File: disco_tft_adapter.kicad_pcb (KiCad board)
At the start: 4 copper layers, 127 x 116.1 mm, 22 parts, among them J1 QTH-030-02-L-D-A, J2 F31L-1A7H1-11030

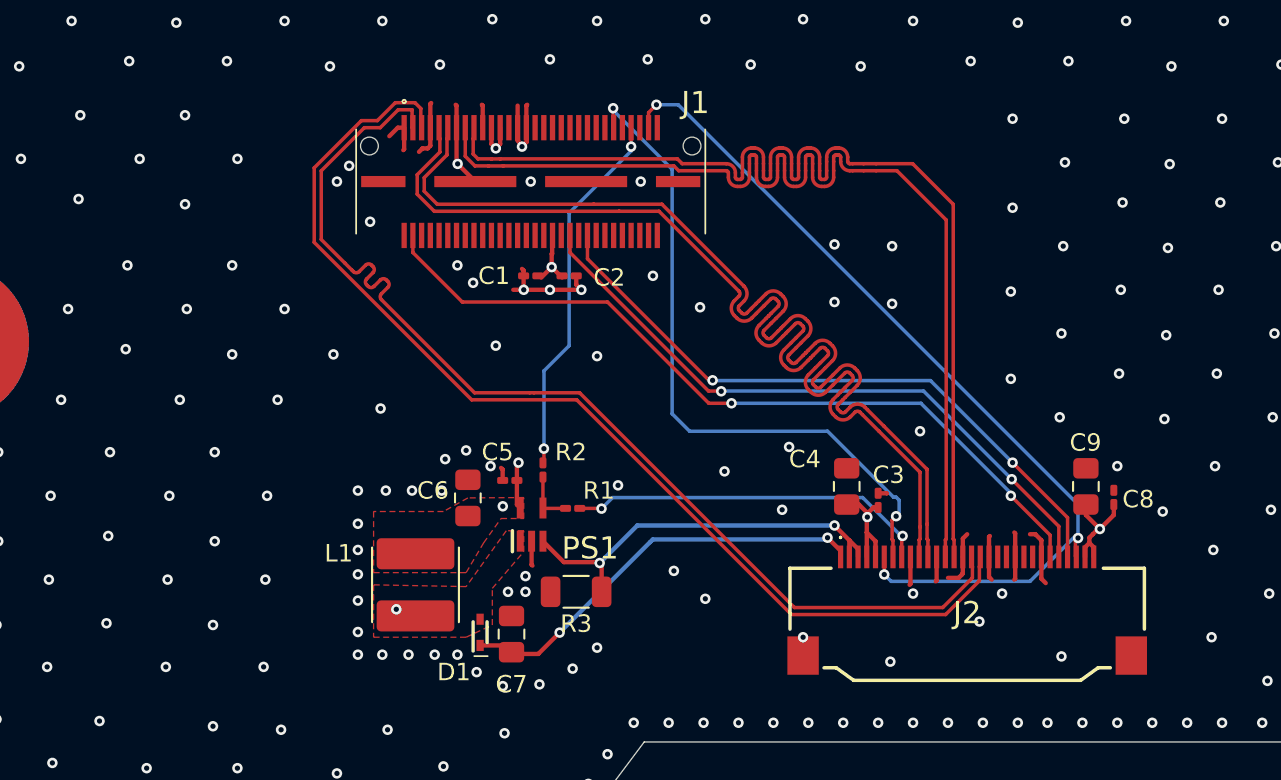
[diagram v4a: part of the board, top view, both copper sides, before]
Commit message: [layout] some finishing touches after gerber review
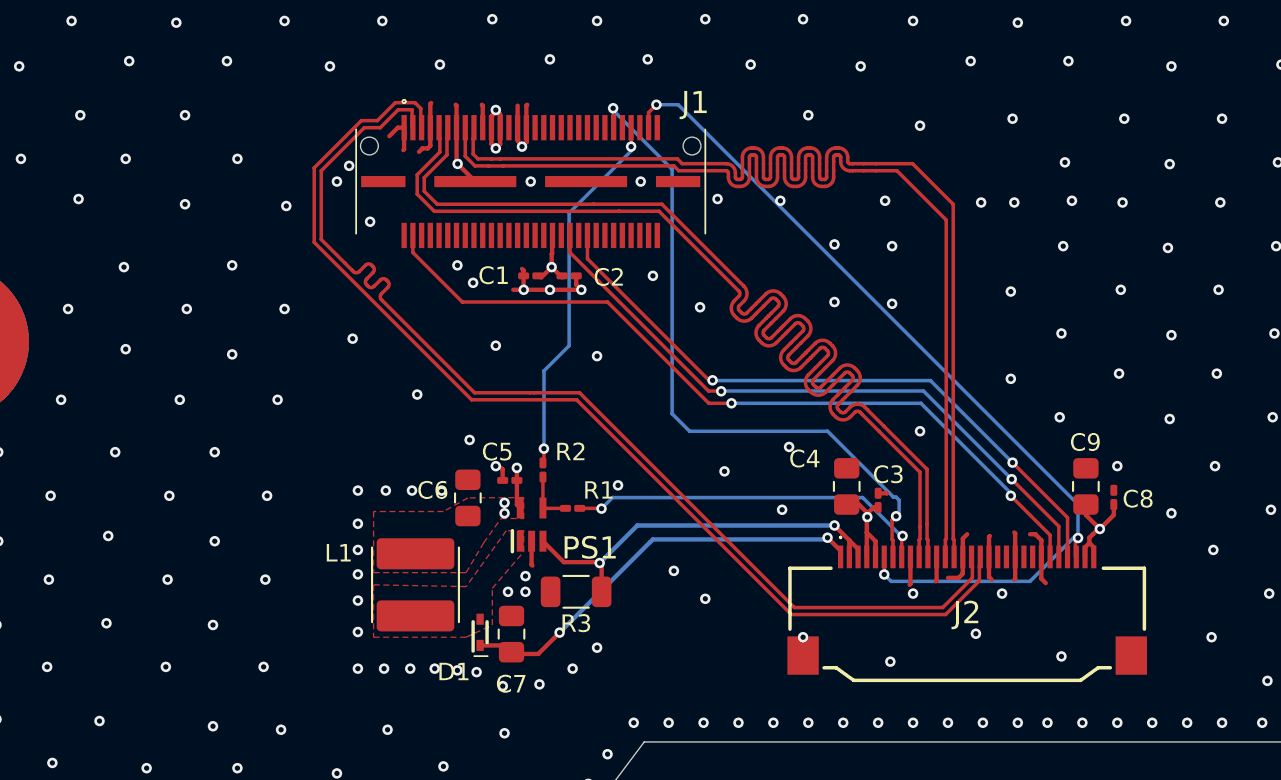
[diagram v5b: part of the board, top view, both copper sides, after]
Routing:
- net VCC_BL: track 5.30 -> 7.19 mm, vias 3 -> 5
- net GND: vias 775 -> 781
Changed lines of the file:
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@@
 			(net 3 "GND")
 			(pintype "passive")
+			(zone_connect 2)
 		)
 		(embedded_fonts no)
@@
 			(net 3 "GND")
 			(pintype "passive")
+			(zone_connect 2)
 		)
 		(embedded_fonts no)
@@
 	)
 	(via
-		(at 72.8 111.5)
+		(at 63.7 97)
 		(size 0.6)
 		(drill 0.3)
@@
 	)
 	(via
-		(at 73.5 122.7)
+		(at 73.5 123.6)
 		(size 0.6)
 		(drill 0.3)
@@
 	)
 	(via
-		(at 69.2 122.7)
+		(at 69.3 123.5)
 		(size 0.6)
 		(drill 0.3)
@@
 	)
 	(via
+		(at 103.5 96.8)
+		(size 0.6)
+		(drill 0.3)
+		(layers "F.Cu" "B.Cu")
+		(free yes)
+		(net 3)
+	)
+	(via
 		(at 49.2 82.2)
 		(size 0.6)
@@
 	)
 	(via
-		(at 72.2 122.7)
+		(at 72.2 123.5)
 		(size 0.6)
 		(drill 0.3)
@@
 	)
 	(via
-		(at 103.4 120.8)
+		(at 103.2 121.5)
 		(size 0.6)
 		(drill 0.3)
@@
 	)
 	(via
+		(at 98 96.7)
+		(size 0.6)
+		(drill 0.3)
+		(layers "F.Cu" "B.Cu")
+		(free yes)
+		(net 3)
+	)
+	(via
 		(at 140.7 126.4)
 		(size 0.6)
@@
 	)
 	(via
-		(at 74 111)
+		(at 74.2 110.4)
 		(size 0.6)
 		(drill 0.3)
@@
 	)
 	(via
-		(at 113.9 114.5)
+		(at 114.4 114.6)
 		(size 0.6)
 		(drill 0.3)
@@
 	)
 	(via
+		(at 88.4 96.6)
+		(size 0.6)
+		(drill 0.3)
+		(layers "F.Cu" "B.Cu")
+		(free yes)
+		(net 3)
+	)
+	(via
 		(at 114.5 79)
 		(size 0.6)
@@
 	)
 	(via
+		(at 100 92.4)
+		(size 0.6)
+		(drill 0.3)
+		(layers "F.Cu" "B.Cu")
+		(free yes)
+		(net 3)
+	)
+	(via
 		(at 152.9 136.2)
 		(size 0.6)
@@
 	)
 	(via
-		(at 114 109.2)
+		(at 114.3 109.2)
 		(size 0.6)
 		(drill 0.3)
@@
 	)
 	(via
-		(at 70.7 122.7)
+		(at 70.8 123.5)
 		(size 0.6)
 		(drill 0.3)
@@
 	)
 	(via
-		(at 55.3 94.3)
+		(at 54.5 94.3)
 		(size 0.6)
 		(drill 0.3)
@@
 	)
 	(via
-		(at 70 120.1)
-		(size 0.6)
-		(drill 0.3)
-		(layers "F.Cu" "B.Cu")
-		(free yes)
-		(net 3)
-	)
-	(via
 		(at 135 131.4)
 		(size 0.6)
@@
 	)
 	(via
-		(at 54.6 100.4)
+		(at 54.4 100.5)
 		(size 0.6)
 		(drill 0.3)
@@
 	)
 	(via
+		(at 108.7 96.7)
+		(size 0.6)
+		(drill 0.3)
+		(layers "F.Cu" "B.Cu")
+		(free yes)
+		(net 3)
+	)
+	(via
 		(at 150.2 94.4)
 		(size 0.6)
@@
 	)
 	(via
-		(at 69.1 108.6)
+		(at 71.2 107.8)
 		(size 0.6)
 		(drill 0.3)
@@
 	)
 	(via
-		(at 105.3 97.1)
+		(at 105.4 96.8)
 		(size 0.6)
 		(drill 0.3)
@@
 	)
 	(via
+		(at 93.6 91.8)
+		(size 0.6)
+		(drill 0.3)
+		(layers "F.Cu" "B.Cu")
+		(free yes)
+		(net 3)
+	)
+	(via
 		(at 140.8 121.6)
 		(size 0.6)
@@
 	)
 	(via
+		(at 92 96.7)
+		(size 0.6)
+		(drill 0.3)
+		(layers "F.Cu" "B.Cu")
+		(free yes)
+		(net 3)
+	)
+	(via
 		(at 150.4 78.3)
 		(size 0.6)
@@
 	)
 	(via
-		(at 75.4 111.9)
+		(at 75.7 111.9)
 		(size 0.6)
 		(drill 0.3)
@@
 	)
 	(via
-		(at 53.6 111.1)
+		(at 53.9 111.1)
 		(size 0.6)
 		(drill 0.3)
@@
 	)
 	(via
-		(at 67.8 122.7)
+		(at 67.8 123.5)
 		(size 0.6)
 		(drill 0.3)
@@
 	)
 	(via
-		(at 114.1 104.4)
+		(at 114.4 104.4)
 		(size 0.6)
 		(drill 0.3)
@@
 	)
 	(via
-		(at 66.4 105.5)
+		(at 67.5 104.6)
 		(size 0.6)
 		(drill 0.3)
@@
 	)
 	(segment
-		(start 76.9075 112.72)
-		(end 76.9075 111.7925)
+		(start 75.7 91.5)
+		(end 75.7 91.6)
 		(width 0.25)
 		(layer "F.Cu")
@@
 	)
 	(segment
-		(start 76.9075 111.7925)
-		(end 77 111.7)
+		(start 76.9075 112)
+		(end 76.9075 112.72)
+		(width 0.25)
+		(layer "F.Cu")
+		(net 20)
+	)
+	(segment
+		(start 75.7 91.6)
+		(end 75.45 91.85)
+		(width 0.25)
+		(layer "F.Cu")
+		(net 20)
+	)
+	(segment
+		(start 75.7 91.5)
+		(end 75.95 91.75)
+		(width 0.25)
+		(layer "F.Cu")
+		(net 20)
+	)
+	(segment
+		(start 75.45 91.85)
+		(end 75.45 92.514)
 		(width 0.25)
 		(layer "F.Cu")
@@
 		(net 20)
 	)
+	(segment
+		(start 75.95 91.75)
+		(end 75.95 92.514)
+		(width 0.25)
+		(layer "F.Cu")
+		(net 20)
+	)
 	(via
-		(at 77 111.7)
+		(at 76.9075 112)
 		(size 0.6)
 		(drill 0.3)
@@
 	)
 	(via
-		(at 76.1 114.2)
+		(at 75.7 91.5)
+		(size 0.6)
+		(drill 0.3)
+		(layers "F.Cu" "B.Cu")
+		(net 20)
+	)
+	(via
+		(at 76.2 114.6)
+		(size 0.6)
+		(drill 0.3)
+		(layers "F.Cu" "B.Cu")
+		(free yes)
+		(net 20)
+	)
+	(via
+		(at 76.2 114)
 		(size 0.6)
 		(drill 0.3)
@@
 		(polygon
 			(pts
-				(xy 69 116.7) (xy 74.7 116.7) (xy 76 115.8) (xy 76 112.6) (xy 78 111.9) (xy 78 110) (xy 76 108.62)
-				(xy 69 108.62)
+				(xy 68.68162 122.3) (xy 74.38162 122.3) (xy 75.68162 121.4) (xy 75.68162 118.2) (xy 77.68162 117.5)
+				(xy 77.68162 115.6) (xy 75.68162 114.22) (xy 68.68162 114.22)
 			)
 		)

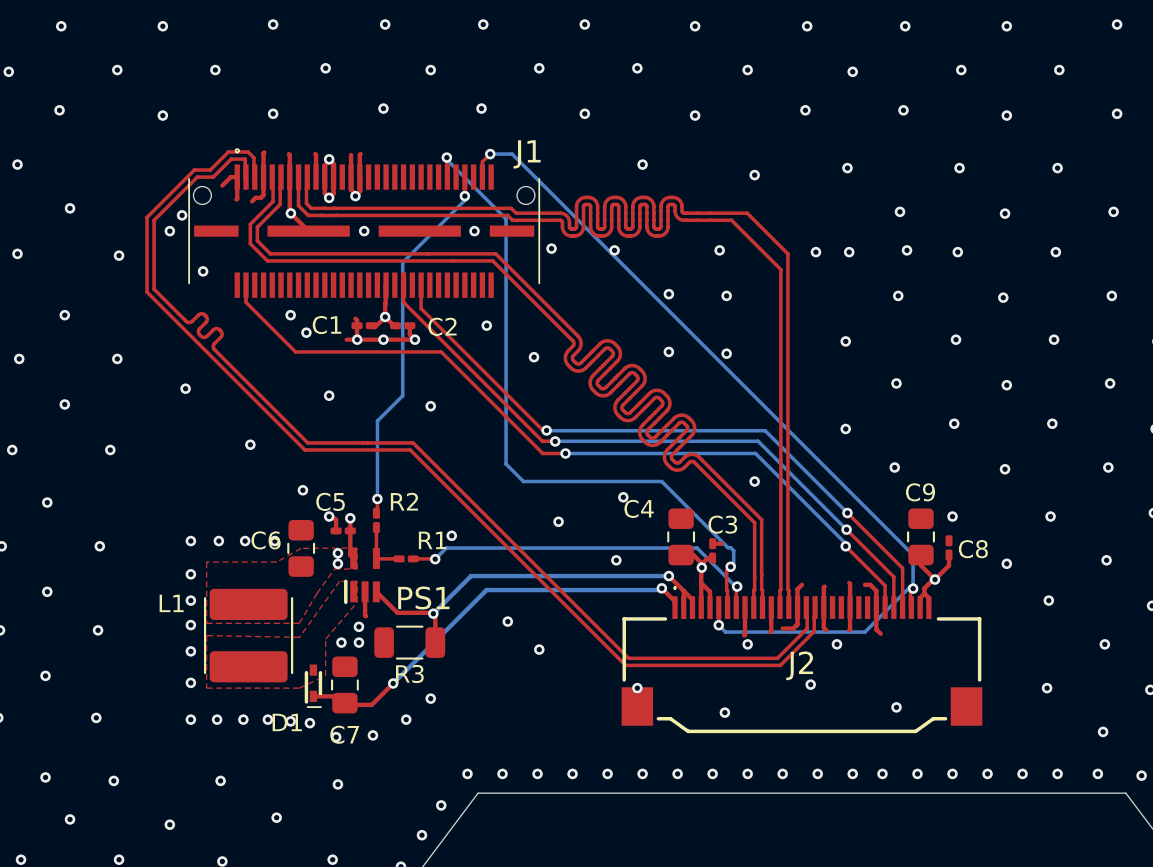
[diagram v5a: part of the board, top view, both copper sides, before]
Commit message: [layout] update footprints, clear routing for tft connector
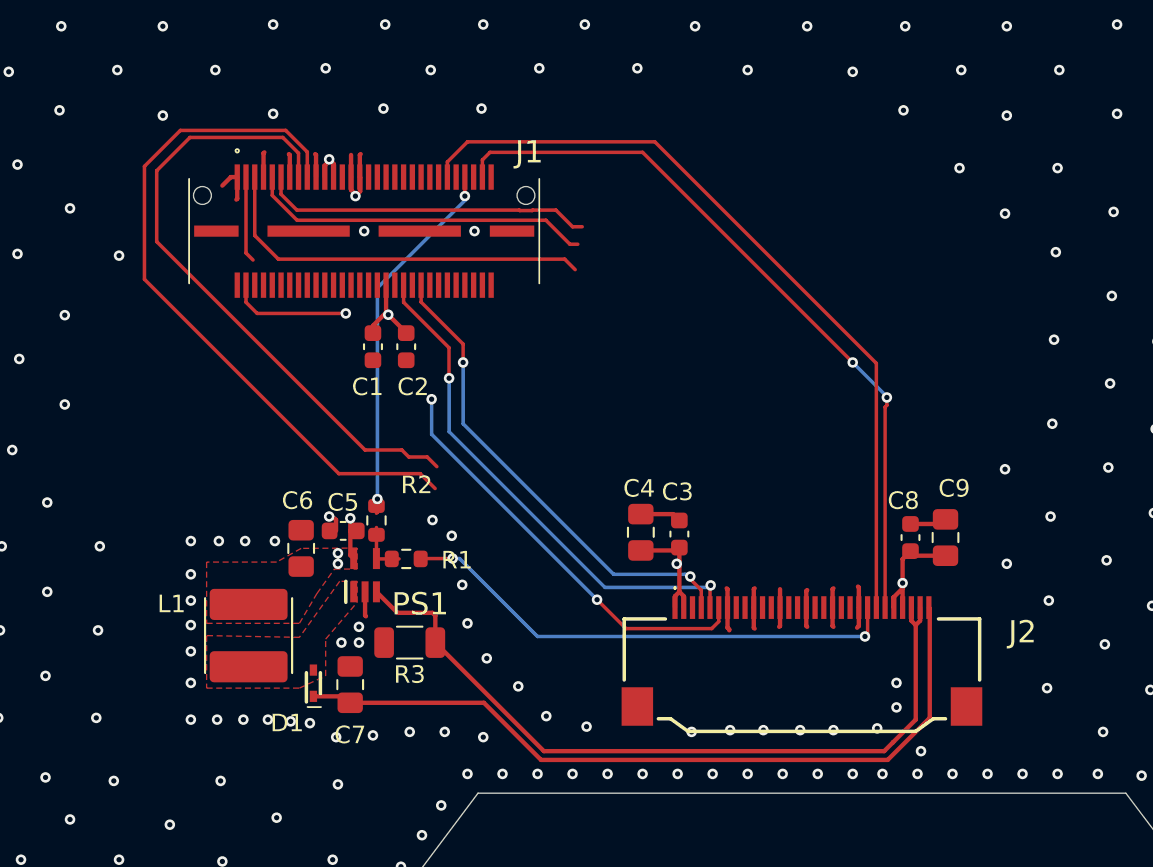
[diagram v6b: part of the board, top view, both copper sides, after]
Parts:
- C1, C2, C3, C5, C8: footprint Capacitor_SMD:C_0201_0603Metric_Pad0.64x0.40mm_HandSolder -> Capacitor_SMD:C_0603_1608Metric
- R1, R2: footprint Resistor_SMD:R_0201_0603Metric_Pad0.64x0.40mm_HandSolder -> Resistor_SMD:R_0603_1608Metric
- moved C4 2.31 mm to (93.5, 112.8)
- moved C8 2.28 mm to (108.9, 113.1)
- moved C3 2.13 mm to (95.7, 112.9)
- moved C9 1.40 mm to (110.9, 113.1)
- moved C1 1.30 mm to (78.2, 102.2), turned to -90 degrees
- moved C2 1.22 mm to (80.1, 102.2), turned to -90 degrees
- moved C7 0.30 mm to (76.9, 121.5)
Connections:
- J2 pad 10: /DSI_D0_P -> unconnected-(J2-Pad10)
- J2 pad 11: /DSI_D0_N -> unconnected-(J2-Pad11)
- J2 pad 13: /DSI_D1_P -> /DSI_D0_P
- J2 pad 14: /DSI_D1_N -> /DSI_D0_N
- J2 pad 22: unconnected-(J2-Pad22) -> /DSI_D1_P
- J2 pad 23: unconnected-(J2-Pad23) -> /DSI_D1_N
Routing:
- net /DSI_CLK_P: track 62.7 -> 4.90 mm
- net /DSI_D0_N: track 62.0 -> 19.0 mm
- net /DSI_D0_P: track 62.0 -> 19.7 mm
- net /DSI_CLK_N: track 62.3 -> 22.4 mm
- net /DSI_D1_P: track 62.4 -> 36.6 mm
- net /DSI_D1_N: track 62.1 -> 40.1 mm
- net /LEDK: track 23.6 -> 43.8 mm, vias 2 -> 0
- net /LEDA: track 24.3 -> 44.0 mm, vias 2 -> 0
- net /CTP_SCL: track 37.4 -> 27.5 mm
- net /RST: track 51.6 -> 42.1 mm, vias 3 -> 2
- net GND: track 40.6 -> 31.9 mm, vias 781 -> 740
- net /PWM_DISP: track 20.9 -> 28.9 mm
- net /CTP_SDA: track 37.2 -> 29.4 mm
- net /CTP_INT: track 45.5 -> 37.8 mm, vias 2 -> 3
- net /TE: track 39.1 -> 45.0 mm, vias 2 -> 0
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
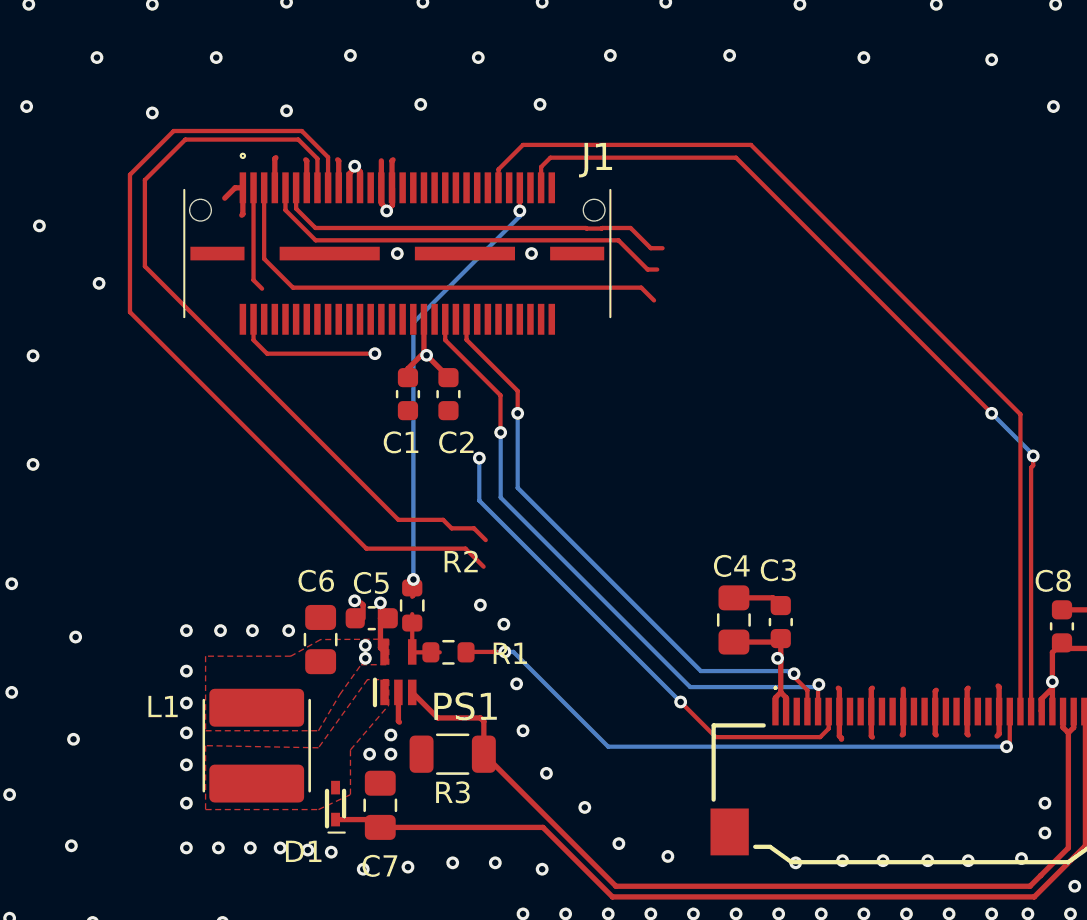
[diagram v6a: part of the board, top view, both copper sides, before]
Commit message: [layout] route display TFT plug
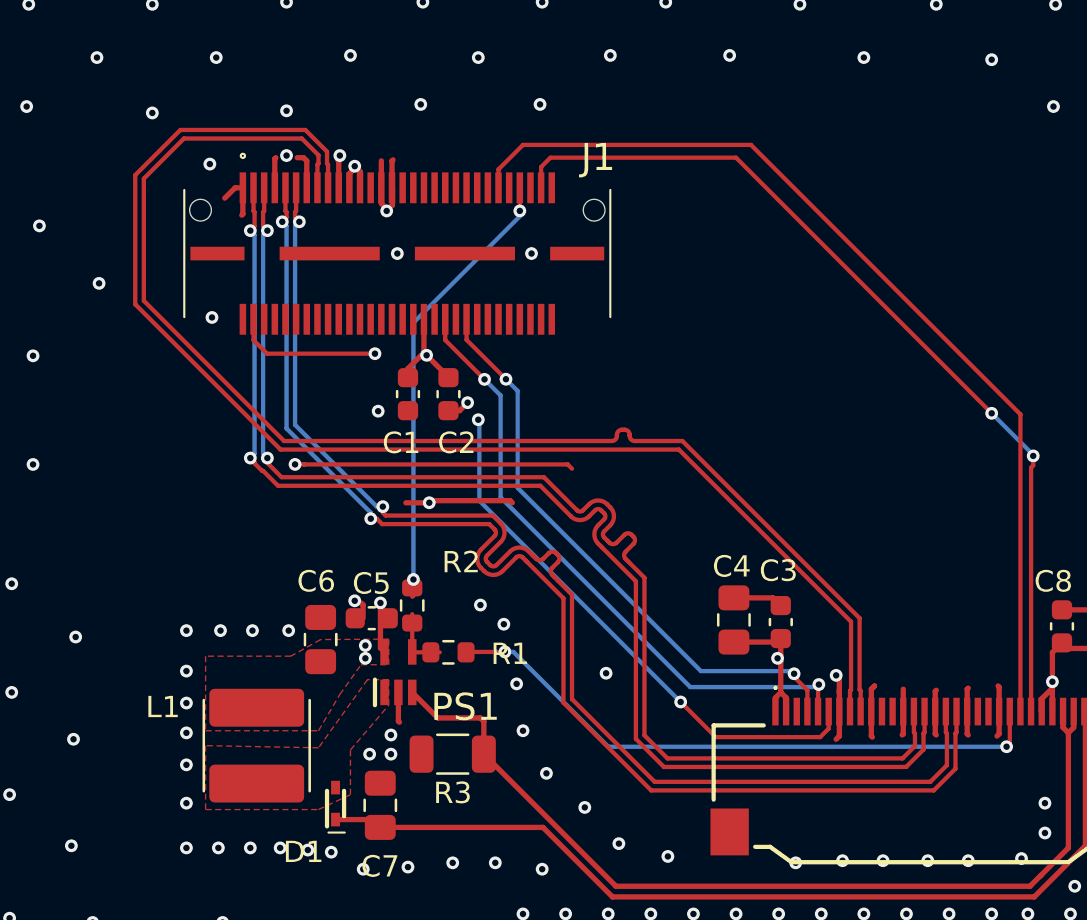
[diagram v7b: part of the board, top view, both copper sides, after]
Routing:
- net /DSI_CLK_P: track 4.90 -> 58.7 mm, vias 0 -> 2
- net /DSI_D0_N: track 19.0 -> 58.7 mm, vias 0 -> 2
- net /DSI_D0_P: track 19.7 -> 58.8 mm, vias 0 -> 2
- net /DSI_CLK_N: track 22.4 -> 58.7 mm, vias 0 -> 2
- net /DSI_D1_P: track 36.6 -> 62.0 mm
- net /DSI_D1_N: track 40.1 -> 62.1 mm
- net GND: track 31.9 -> 52.9 mm, vias 740 -> 750
- net /CTP_INT: track 37.8 -> 38.9 mm
